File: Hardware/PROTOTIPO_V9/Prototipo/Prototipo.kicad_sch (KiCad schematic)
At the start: 1 part, among them U1 YAAJ_BluePill_Part_Like_SWD_B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

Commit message: Esquematico TR V 1 ,2 & 3
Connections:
- net ZMPT101B/OUT_TR_V_3: now reaches U1.10 (PA15)
- net ZMPT101B/OUT_TR_V_1: now reaches U1.8 (PA11)
- net ZMPT101B/OUT_TR_V_2: now reaches U1.9 (PA12)
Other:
- sheet ZMPT101B ports: added OUT_TR_V_1, OUT_TR_V_2, OUT_TR_V_3; removed none
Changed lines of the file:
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@@
 	(generator_version "9.0")
 	(paper "A4")
+	(wire
+		(pts
+			(xy 107.95 83.82) (xy 116.84 83.82)
+		)
+		(stroke
+			(width 0)
+			(type default)
+		)
+	)
+	(wire
+		(pts
+			(xy 109.22 69.85) (xy 109.22 81.28)
+		)
+		(stroke
+			(width 0)
+			(type default)
+		)
+	)
+	(wire
+		(pts
+			(xy 107.95 72.39) (xy 107.95 83.82)
+		)
+		(stroke
+			(width 0)
+			(type default)
+		)
+	)
+	(wire
+		(pts
+			(xy 72.39 69.85) (xy 109.22 69.85)
+		)
+		(stroke
+			(width 0)
+			(type default)
+		)
+	)
+	(wire
+		(pts
+			(xy 110.49 67.31) (xy 110.49 78.74)
+		)
+		(stroke
+			(width 0)
+			(type default)
+		)
+	)
+	(wire
+		(pts
+			(xy 72.39 72.39) (xy 107.95 72.39)
+		)
+		(stroke
+			(width 0)
+			(type default)
+		)
+	)
+	(wire
+		(pts
+			(xy 110.49 78.74) (xy 116.84 78.74)
+		)
+		(stroke
+			(width 0)
+			(type default)
+		)
+	)
+	(wire
+		(pts
+			(xy 109.22 81.28) (xy 116.84 81.28)
+		)
+		(stroke
+			(width 0)
+			(type default)
+		)
+	)
+	(wire
+		(pts
+			(xy 72.39 67.31) (xy 110.49 67.31)
+		)
+		(stroke
+			(width 0)
+			(type default)
+		)
+	)
 	(symbol
 		(lib_id "YAAJ_BluePill_Part_Like_SWD_Breakout:YAAJ_BluePill_Part_Like_SWD_Breakout")
@@
 			)
 		)
+		(pin "OUT_TR_V_3" output
+			(at 72.39 72.39 0)
+			(effects
+				(font
+					(size 1.27 1.27)
+				)
+				(justify right)
+			)
+		)
+		(pin "OUT_TR_V_2" output
+			(at 72.39 69.85 0)
+			(effects
+				(font
+					(size 1.27 1.27)
+				)
+				(justify right)
+			)
+		)
+		(pin "OUT_TR_V_1" output
+			(at 72.39 67.31 0)
+			(effects
+				(font
+					(size 1.27 1.27)
+				)
+				(justify right)
+			)
+		)

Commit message: Esquematico RTC
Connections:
- net DS3231/RTC_SCL: now reaches U1.14 (PB6)
- net DS3231/RTC_SDA: now reaches U1.15 (PB7)
- net GND: now reaches U1.19 (GND)
- net GND: now also U1.39 (GND), U1.40 (GND)
- net +3V3: now reaches U1.20 (3V3)
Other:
- sheet FUENTE renamed HLK5M05
- sheet DS3231 ports: added RTC_SCL, RTC_SDA; removed none
- sheet HLK5M05 ports: added 220VAC_L, 220VAC_N; removed none
- sheet ZMPT101B ports: added 220VAC_L, 220VAC_N; removed none

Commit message: Esquematico Encoder
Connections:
- net ENCODER/ENC_SW: now reaches U1.4 (PB15)
- net ENCODER/ENC_DT: now reaches U1.5 (PA8)
- net ENCODER/ENC_CLK: now reaches U1.6 (PA9)
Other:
- sheet ENCODER ports: added ENC_CLK, ENC_DT, ENC_SW; removed none
- moved on the sheet: U1

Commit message: Libreria actualizada
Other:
- sheet ENCODER renamed KY040
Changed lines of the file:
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@@
 			(color 0 0 0 0.0000)
 		)
-		(property "Sheetname" "ENCODER"
+		(property "Sheetname" "KY040"
 			(at 36.83 67.8684 0)
 			(effects

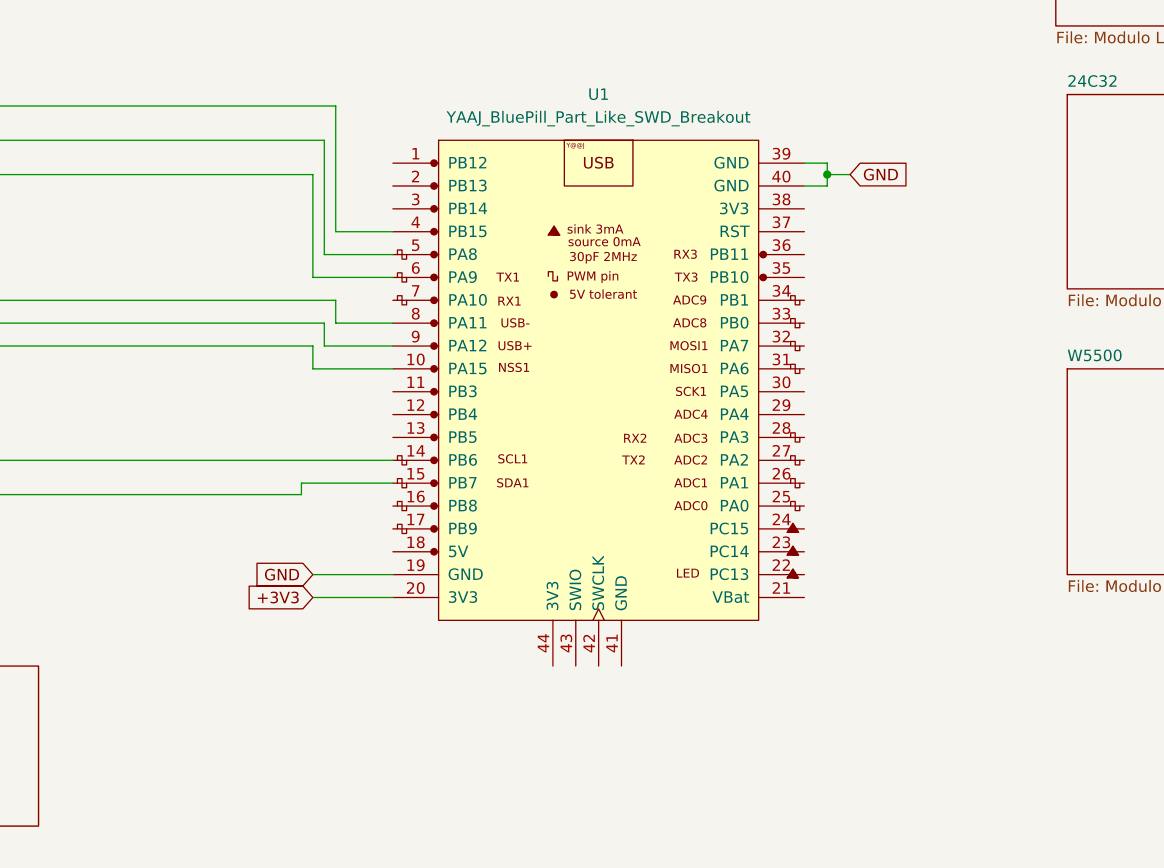
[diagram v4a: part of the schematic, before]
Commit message: Se agrega sch/fp W5500, ILI9341 y fp BluePill
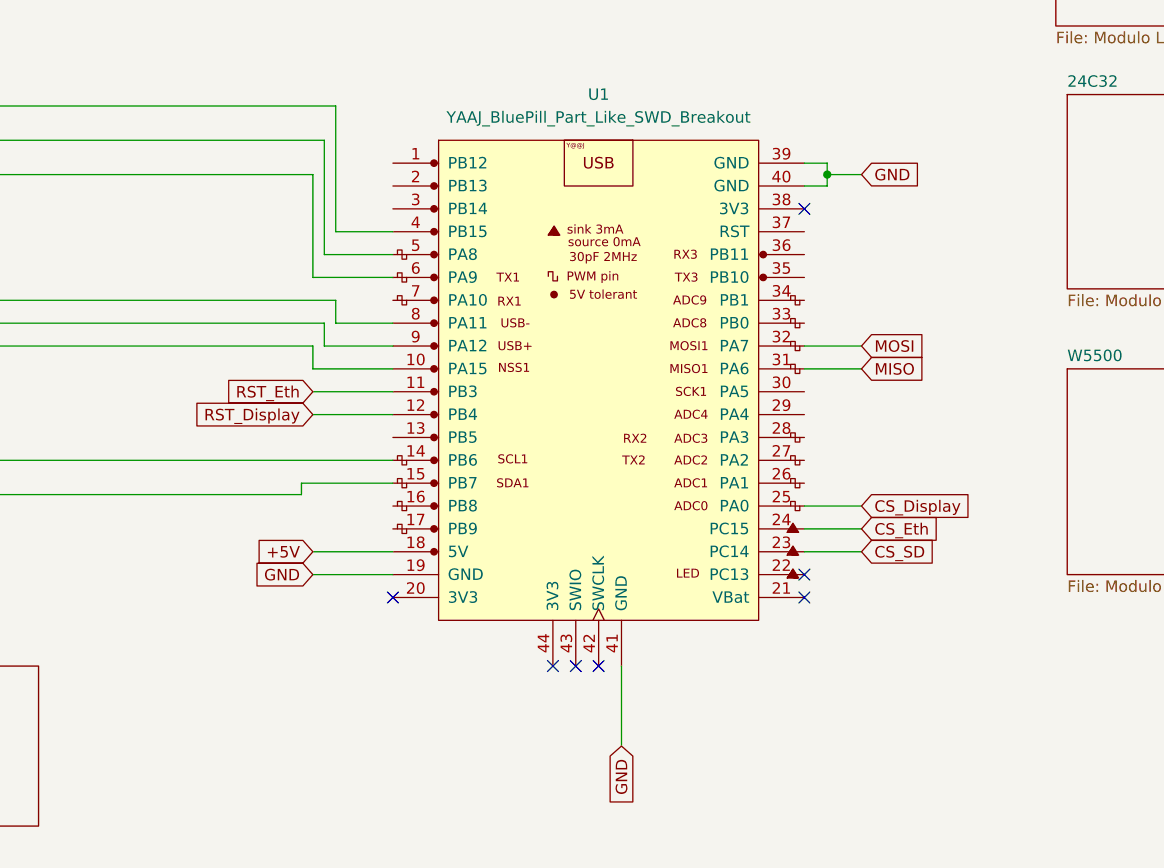
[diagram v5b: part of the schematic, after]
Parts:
- U1: footprint Kicad-STM32:YAAJ_BluePill_TOP -> footprints_proyecto:YAAJ_BluePill_1
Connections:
- net GND: now also U1.41 (GND)
- net RST_Eth: now reaches U1.11 (PB3)
- net RST_Display: now reaches U1.12 (PB4)
- net +5V: now reaches U1.18 (5V)
- net CS_SD: now reaches U1.23 (PC14)
- net CS_Eth: now reaches U1.24 (PC15)
- net CS_Display: now reaches U1.25 (PA0)
- net MISO: now reaches U1.31 (PA6)
- net MOSI: now reaches U1.32 (PA7)
- net +3V3: no longer names the net of U1.20 (3V3)
- no-connect marks 0 -> 7

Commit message: Bus de salida
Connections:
- net PCB2CONNECTION/BUS_ENC_DT: now reaches U1.7 (PA10)
- net CS_Display renamed PCB2CONNECTION/BUS_LCD_CS
- net KY040/ENC_CLK renamed PCB2CONNECTION/BUS_ENC_SW
- net KY040/ENC_DT renamed PCB2CONNECTION/BUS_ENC_CLK
- net KY040/ENC_SW: no longer names the net of U1.4 (PB15)
- net RST_Display renamed PCB2CONNECTION/BUS_LCD_RST
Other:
- removed sheet ILI9341
- removed sheet KY040
- added sheet PCB2CONNECTION (CONN_BUS.kicad_sch)
